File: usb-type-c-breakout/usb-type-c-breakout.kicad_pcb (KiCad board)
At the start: 4 copper layers, 29.5 x 47.5 mm, 34 parts, among them J10 USB_B_Micro, J11 USB_C_Plug, J12 Conn_02x04_Odd_Even, J2 Conn_Coaxial, J3 Conn_Coaxial, J4 Conn_Coaxial, J5 Conn_Coaxial, J6 Conn_Coaxial, J7 Conn_Coaxial, J8 Conn_Coaxial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

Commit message: two example diff pairs routed
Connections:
- REF** pad 1: Net-(J10-Pad2) -> Net-(J11-PadA2)
- REF** pad 1: (no net) -> Net-(J11-PadA2)
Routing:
- net Net-(J11-PadA3): track 0.00 -> 17.5 mm
- net Net-(J11-PadA2): track 1.70 -> 17.5 mm
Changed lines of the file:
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@@
     (thickness 1.6)
     (drawings 4)
-    (tracks 21)
+    (tracks 30)
     (modules 34)
     (nets 22)
@@
     )
     (pad "1" smd custom (at 0 1 90) (size 0.3 0.3) (layers "F.Cu")
+      (net 1 "Net-(J11-PadA2)")
       (options (clearance outline) (anchor circle))
       (primitives
         (gr_arc (start 0 -1) (end 0 0) (angle -90) (width 0.3))
       ))
-    (pad "1" smd circle (at 1 0 90) (size 0.3 0.3) (layers "F.Cu"))
+    (pad "1" smd circle (at 1 0 90) (size 0.3 0.3) (layers "F.Cu")
+      (net 1 "Net-(J11-PadA2)"))
   )
   (module "footprint:arc1_00mm" (layer "F.Cu")
@@
     )
     (pad "1" smd custom (at 0 0.75 270) (size 0.3 0.3) (layers "F.Cu")
-      (net 15 "Net-(J10-Pad2)")
+      (net 1 "Net-(J11-PadA2)")
       (options (clearance outline) (anchor circle))
       (primitives
@@
       ))
     (pad "1" smd circle (at 0.75 0 270) (size 0.3 0.3) (layers "F.Cu")
-      (net 15 "Net-(J10-Pad2)"))
+      (net 1 "Net-(J11-PadA2)"))
   )
   (module "Resistor_SMD:R_0603_1608Metric" (layer "B.Cu")
@@
   (gr_line (start 114.75 76.25) (end 114.75 123.75) (layer "Edge.Cuts") (width 0.05))
   (gr_line (start 85.25 76.25) (end 114.75 76.25) (layer "Edge.Cuts") (width 0.05))
+  (segment (start 88 82) (end 91.5 82) (width 0.3) (layer "F.Cu") (net 1))
+  (segment (start 92.5 83) (end 92.5 86.75) (width 0.3) (layer "F.Cu") (net 1))
+  (segment (start 88 94) (end 91.5 94) (width 0.3) (layer "F.Cu") (net 2))
+  (segment (start 92.5 93) (end 92.5 89.25) (width 0.3) (layer "F.Cu") (net 2))
+  (segment (start 94.75 89) (end 94.75 97) (width 0.3) (layer "F.Cu") (net 2))
+  (segment (start 94 88.25) (end 93.5 88.25) (width 0.3) (layer "F.Cu") (net 2))
+  (segment (start 93.5 87.75) (end 94 87.75) (width 0.3) (layer "F.Cu") (net 1))
+  (segment (start 95.25 97) (end 95.25 89) (width 0.3) (layer "F.Cu") (net 1))
+  (segment (start 97.7 98.25) (end 96 98.25) (width 0.27) (layer "F.Cu") (net 2))
   (segment (start 105.25 97) (end 105.25 89) (width 0.3) (layer "F.Cu") (net 7))
   (segment (start 106.5 87.75) (end 106 87.75) (width 0.3) (layer "F.Cu") (net 8))

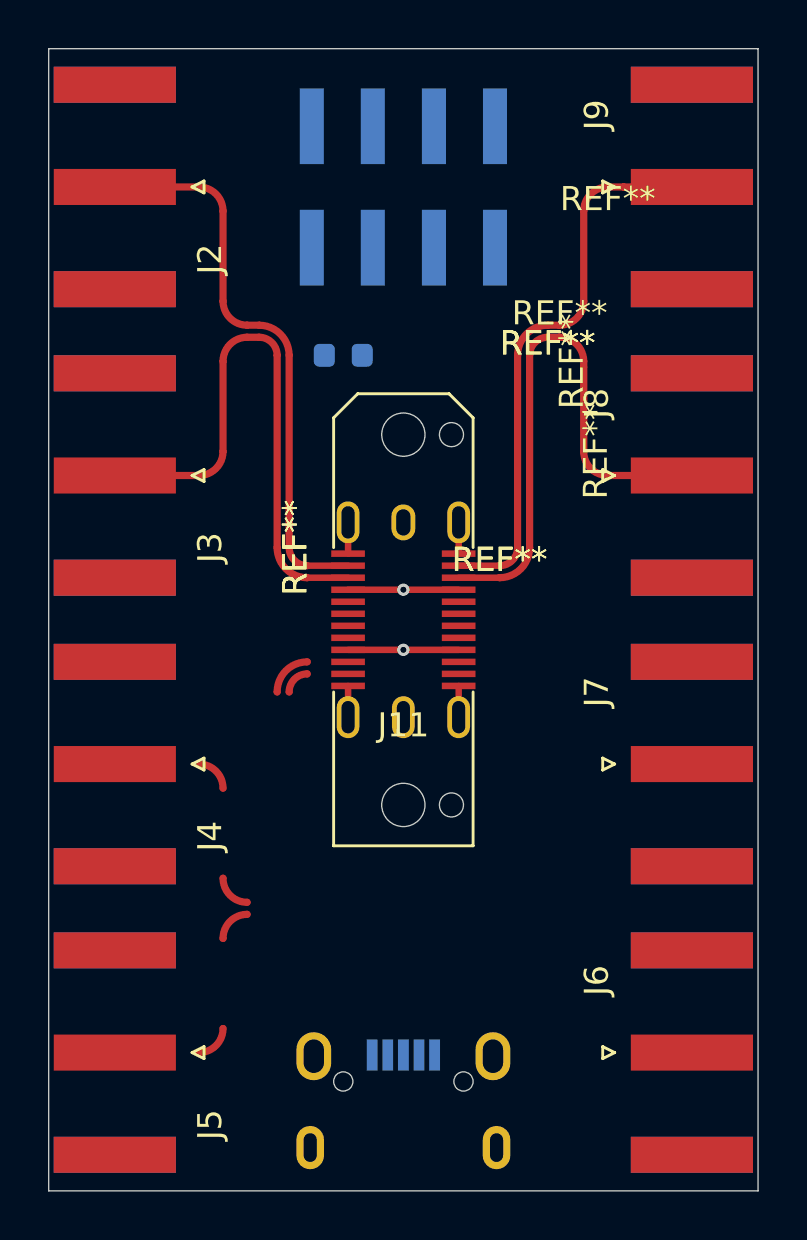
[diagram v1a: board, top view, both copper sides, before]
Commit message: all diff traces routed, pins broken out
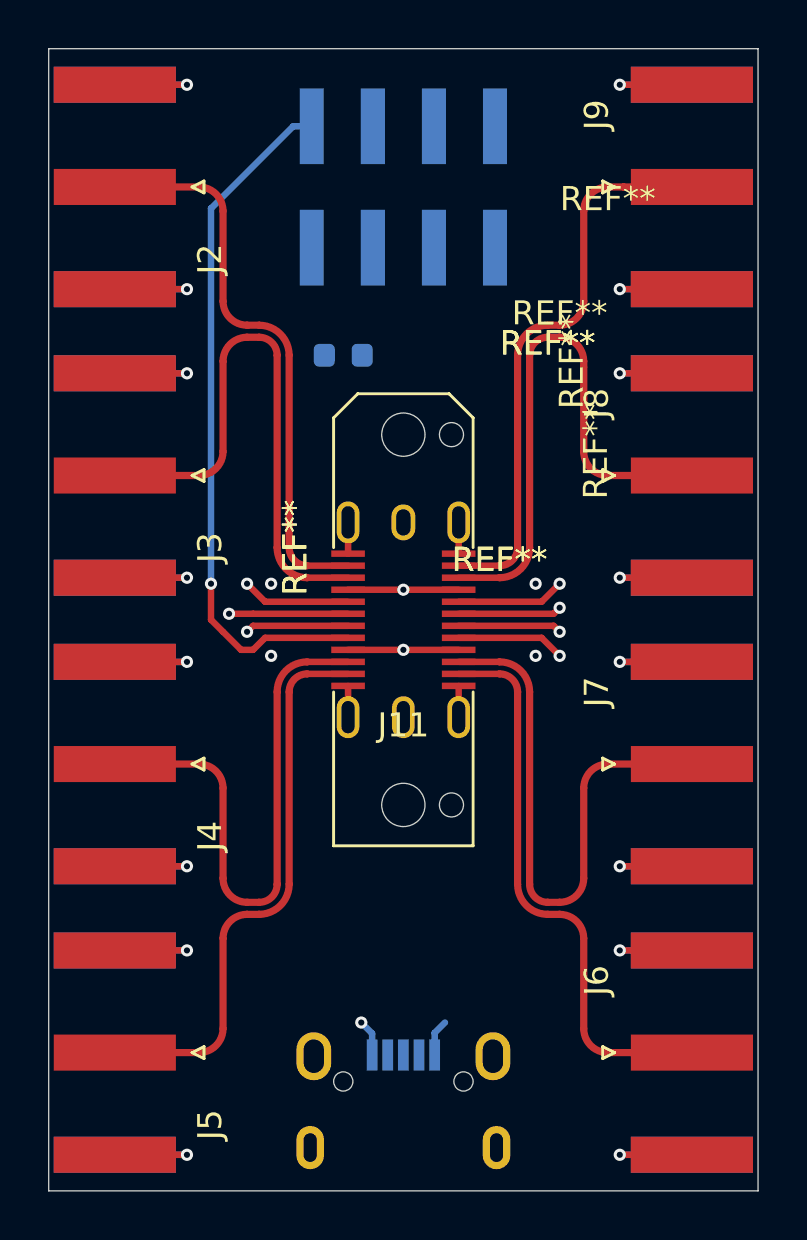
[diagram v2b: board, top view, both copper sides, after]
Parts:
- added REF**: arc0_75mm, footprint:arc0_75mm, F.Cu at (106.0, 111.0)
- added REF**: arc1_25mm, footprint:arc1_25mm, F.Cu at (94.0, 111.0)
- added REF**: arc1_25mm, footprint:arc1_25mm, F.Cu at (106.0, 111.0)
- added REF**: arc1_25mm, footprint:arc1_25mm, F.Cu at (104.0, 103.0)
- added REF**: arc0_75mm, footprint:arc0_75mm, F.Cu at (104.0, 103.0)
- added REF**: arc1_00mm, footprint:arc1_00mm, F.Cu at (106.5, 110.8)
- added REF**: arc1_00mm, footprint:arc1_00mm, F.Cu at (106.5, 113.2)
- added REF**: arc1_00mm, footprint:arc1_00mm, F.Cu at (108.5, 107.0)
- added REF**: arc1_00mm, footprint:arc1_00mm, F.Cu at (108.5, 117.0)
- added REF**: arc0_75mm, footprint:arc0_75mm, F.Cu at (94.0, 111.0)
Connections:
- REF** pad 1: (no net) -> Net-(J11-PadA10) (x3)
- REF** pad 1: (no net) -> Net-(J11-PadA11) (x3)
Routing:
- net Net-(J10-Pad5): track 0.00 -> 73.5 mm, vias 0 -> 13
- net Net-(J11-PadA8): track 0.00 -> 29.1 mm, vias 0 -> 1
- net Net-(J6-Pad2): track 0.00 -> 24.0 mm, vias 0 -> 4
- net Net-(J11-PadB3): track 0.00 -> 17.5 mm
- net Net-(J11-PadB2): track 0.00 -> 17.5 mm
- net Net-(J11-PadA11): track 0.00 -> 17.5 mm
- net Net-(J11-PadA10): track 0.00 -> 17.5 mm
- net Net-(J10-Pad3): track 0.00 -> 4.95 mm, vias 0 -> 1
- net Net-(J11-PadB8): track 0.00 -> 4.51 mm, vias 0 -> 1
- net Net-(J11-PadB5): track 0.00 -> 4.51 mm, vias 0 -> 1
- net /CC: track 0.00 -> 4.51 mm, vias 0 -> 1
- net Net-(J11-PadB7): track 0.00 -> 4.30 mm, vias 0 -> 1
- net Net-(J11-PadB6): track 0.00 -> 4.30 mm, vias 0 -> 1
- net Net-(J10-Pad2): track 0.00 -> 4.30 mm, vias 0 -> 1
- net /VBUS: track 9.20 -> 10.7 mm
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
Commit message: routed USB signals
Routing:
- net Net-(J10-Pad3): track 4.95 -> 26.3 mm
- net Net-(J10-Pad2): track 4.30 -> 25.1 mm
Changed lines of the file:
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@@
     (thickness 1.6)
     (drawings 4)
-    (tracks 138)
+    (tracks 146)
     (modules 44)
     (nets 22)
@@
   (gr_line (start 114.75 76.25) (end 114.75 123.75) (layer "Edge.Cuts") (width 0.05))
   (gr_line (start 85.25 76.25) (end 114.75 76.25) (layer "Edge.Cuts") (width 0.05))
+  (segment (start 93.25 108.75) (end 100.65 116.15) (width 0.27) (layer "B.Cu") (net 15))
+  (segment (start 93.246001 100.753999) (end 93.25 100.757998) (width 0.27) (layer "B.Cu") (net 15))
+  (segment (start 93.25 100.757998) (end 93.25 108.75) (width 0.27) (layer "B.Cu") (net 15))
+  (segment (start 93.5 100.5) (end 93.246001 100.753999) (width 0.27) (layer "B.Cu") (net 15))
+  (segment (start 100.65 116.15) (end 100.65 118.1) (width 0.27) (layer "B.Cu") (net 15))
+  (segment (start 92.75 109) (end 100 116.25) (width 0.27) (layer "B.Cu") (net 16))
+  (segment (start 100 116.25) (end 100 118.1) (width 0.27) (layer "B.Cu") (net 16))
+  (segment (start 92.75 99.75) (end 92.75 109) (width 0.27) (layer "B.Cu") (net 16))
   (segment (start 101.3 118.1) (end 101.3 117.18) (width 0.27) (layer "B.Cu") (net 19))
   (segment (start 101.3 117.18) (end 101.73 116.75) (width 0.27) (layer "B.Cu") (net 19))

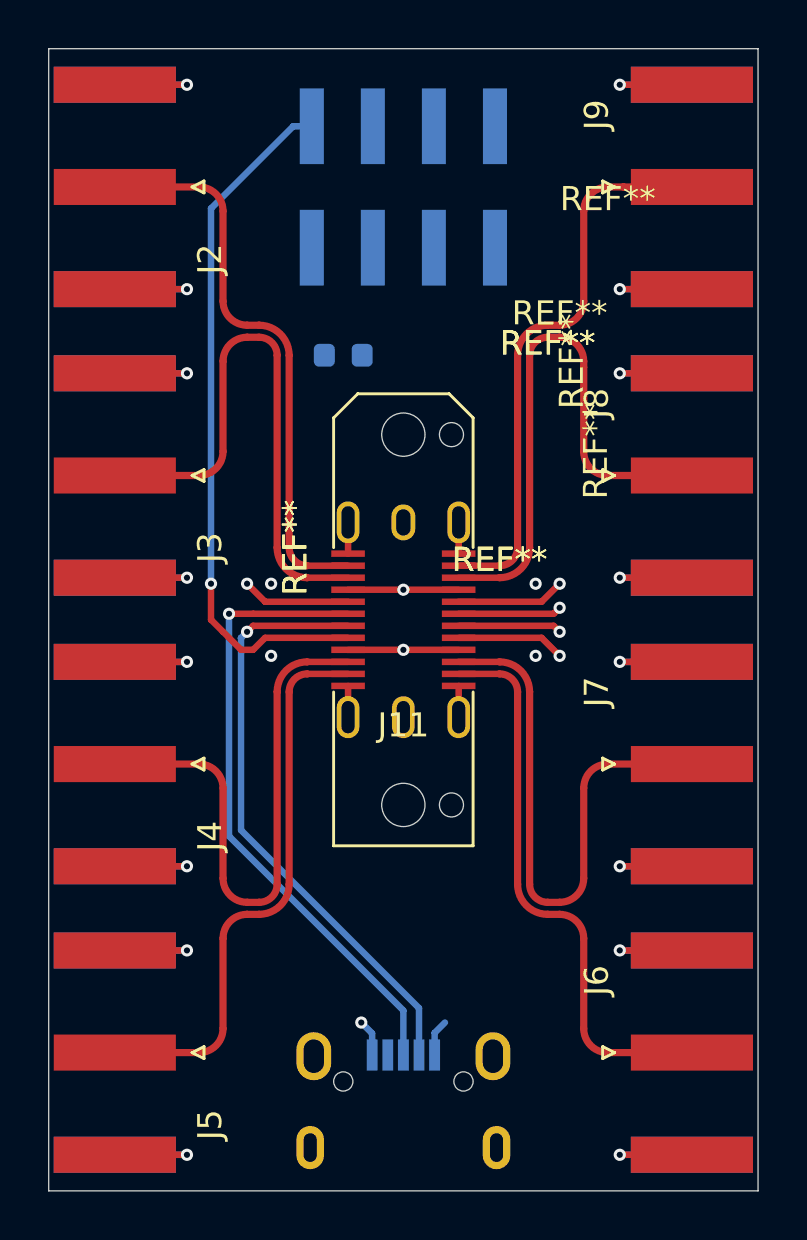
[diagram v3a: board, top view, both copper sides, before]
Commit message: fully connected, with poured planes
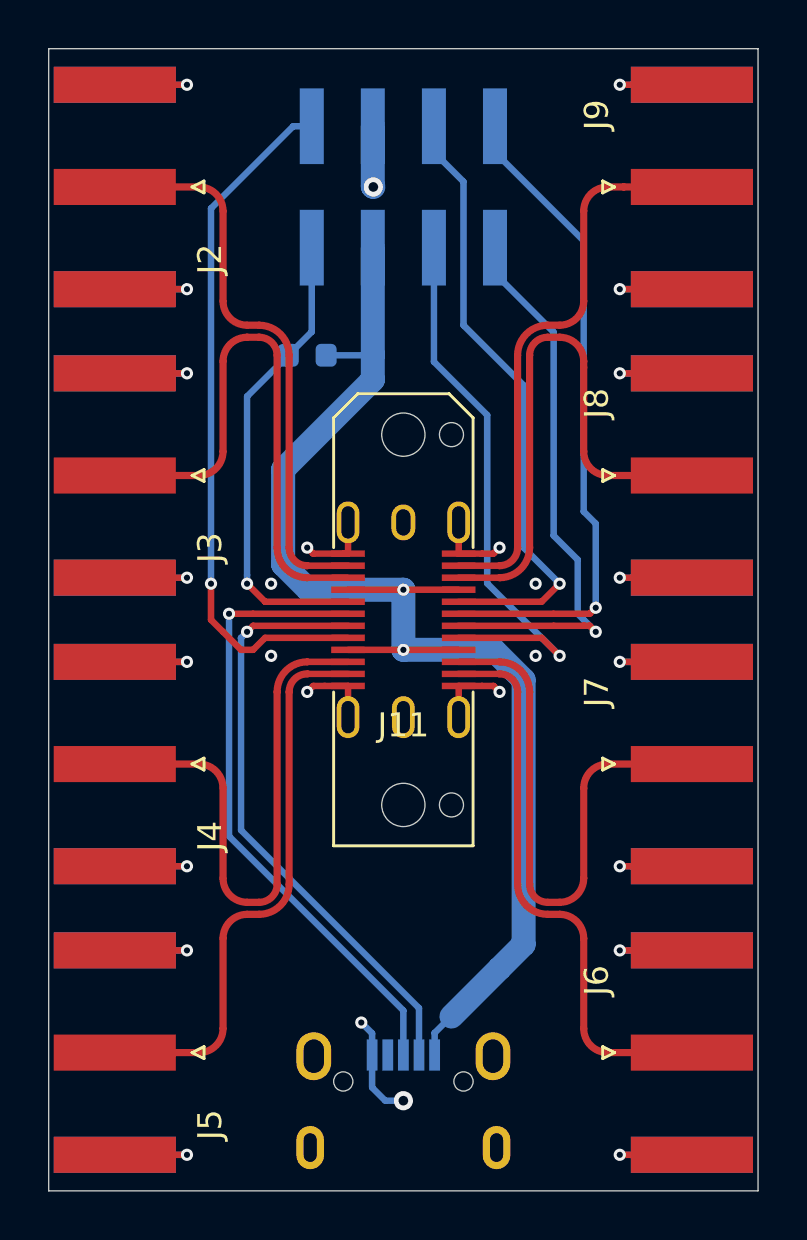
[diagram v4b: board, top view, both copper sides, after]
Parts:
- moved R1 1.50 mm to (96.0, 89.0)
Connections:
- J10 pad 5: Net-(J10-Pad5) -> /GND
- J10 pad 6: Net-(J10-Pad5) -> /GND
- J2 pad 2: Net-(J10-Pad5) -> /GND
- J3 pad 2: Net-(J10-Pad5) -> /GND
- J4 pad 2: Net-(J10-Pad5) -> /GND
- J5 pad 2: Net-(J10-Pad5) -> /GND
- J6 pad 2: Net-(J6-Pad2) -> /GND
- J7 pad 2: Net-(J6-Pad2) -> /GND
- J8 pad 2: Net-(J10-Pad5) -> /GND
- J9 pad 2: Net-(J10-Pad5) -> /GND
- REF** pad 1: Net-(J11-PadB11) -> (no net) (x4)
- REF** pad 1: Net-(J11-PadA11) -> (no net) (x4)
- REF** pad 1: Net-(J11-PadA10) -> (no net) (x4)
- REF** pad 1: Net-(J11-PadA3) -> (no net) (x4)
- REF** pad 1: Net-(J11-PadA2) -> (no net) (x4)
- REF** pad 1: Net-(J11-PadB2) -> (no net) (x4)
- REF** pad 1: Net-(J11-PadB3) -> (no net) (x4)
- REF** pad 1: Net-(J11-PadB10) -> (no net) (x4)
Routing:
- net /GND: track 5.20 -> 115.4 mm, vias 0 -> 27
- net Net-(J10-Pad5): track 73.5 -> 0.00 mm, vias 13 -> 0
- net /VBUS: track 10.7 -> 56.5 mm
- net Net-(J6-Pad2): track 24.0 -> 0.00 mm, vias 4 -> 0
- net Net-(J11-PadB7): track 4.30 -> 27.6 mm
- net Net-(J11-PadB8): track 4.51 -> 25.7 mm
- net Net-(J11-PadB6): track 4.30 -> 23.5 mm
- net Net-(J11-PadB5): track 4.51 -> 23.7 mm
- net /CC: track 4.51 -> 19.6 mm
- net (no net): vias 4 -> 0
- added copper zone on In1.Cu, net /GND
- added copper zone on In2.Cu, net /GND

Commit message: added cutouts under SMA signal pad
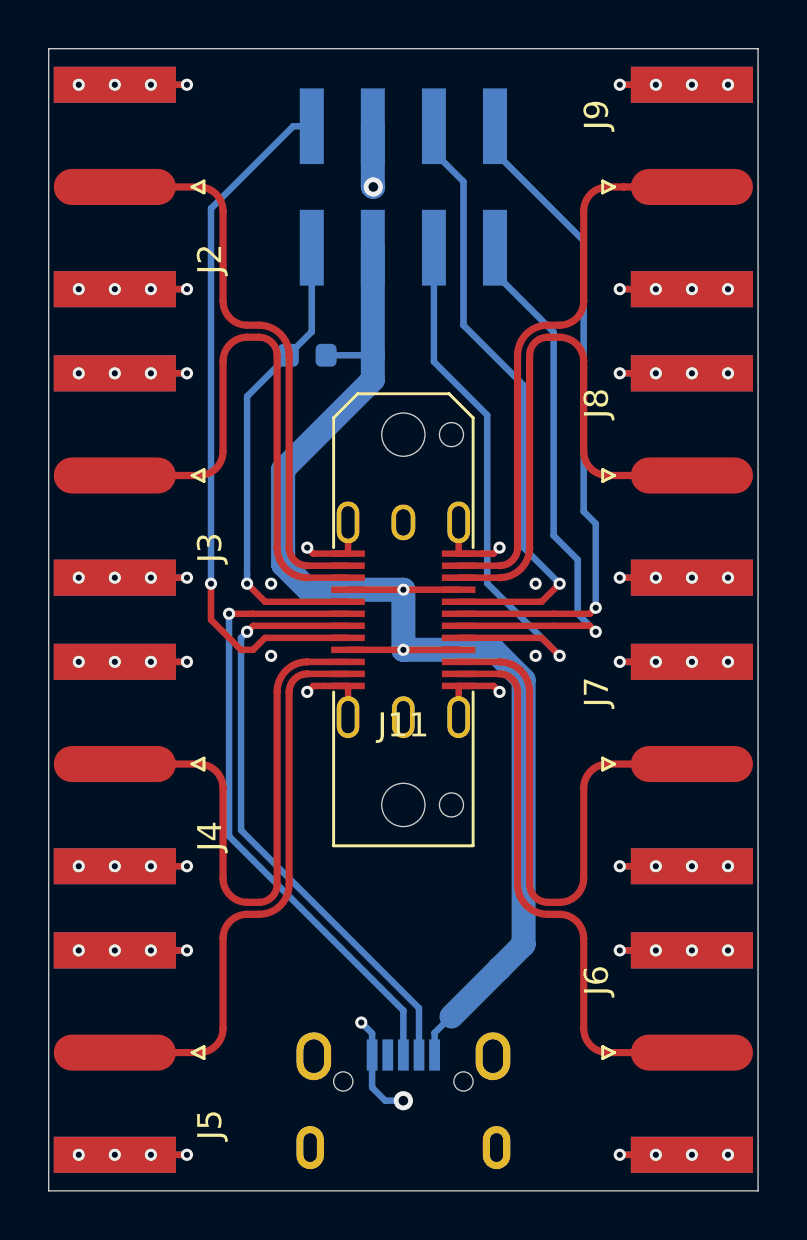
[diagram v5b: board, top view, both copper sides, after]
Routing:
- net /GND: vias 27 -> 75
